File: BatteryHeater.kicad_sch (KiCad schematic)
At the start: 17 parts, among them Q5 SIRA99DP-T1-GE3, Q6 IRLML2803

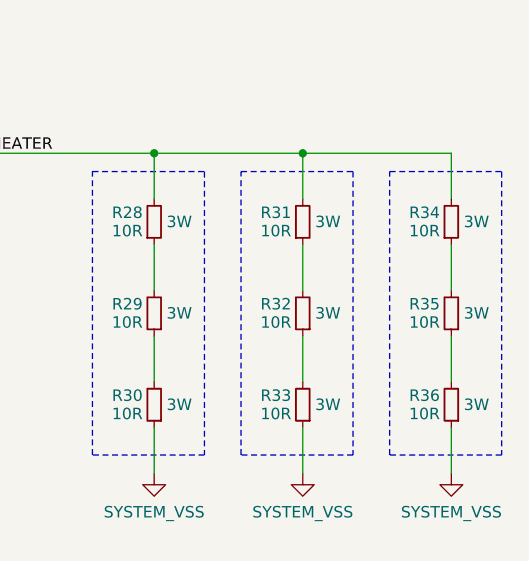
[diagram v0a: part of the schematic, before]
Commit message: Updates board to 2s2p configuration.
Removes 2 cells from Battery, 2 thermistors from Battery Monitor, and 2 heater from BatteryHeater an BatteryHeater1
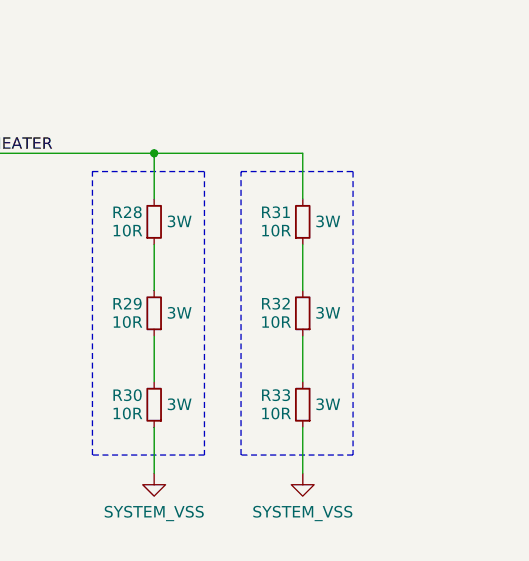
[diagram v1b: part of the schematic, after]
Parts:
- removed R34, R35, R36: 10R, Resistor_SMD:R_2512_6332Metric, symbol Device:R_Small
